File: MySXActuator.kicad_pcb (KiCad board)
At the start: 2 copper layers, 27.7 x 44 mm, 40 parts, among them J1 8P8C, Q1 2N7002, Q2 IRFR7546PbF, Q3 IRFR7546PbF, Q4 2N7002, Q5 BSS84A, U1 AP63205WU

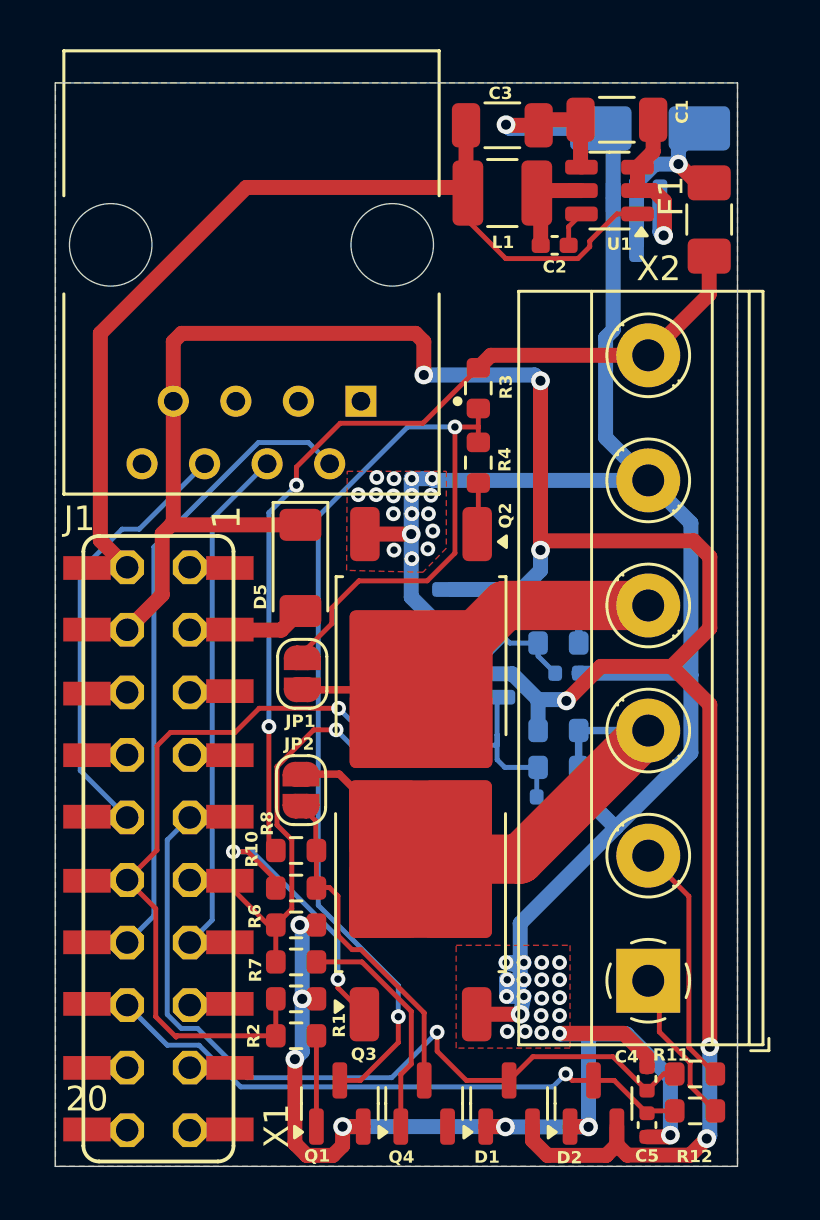
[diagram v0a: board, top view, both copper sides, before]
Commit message: add resistors to prevent led glowing when turned off
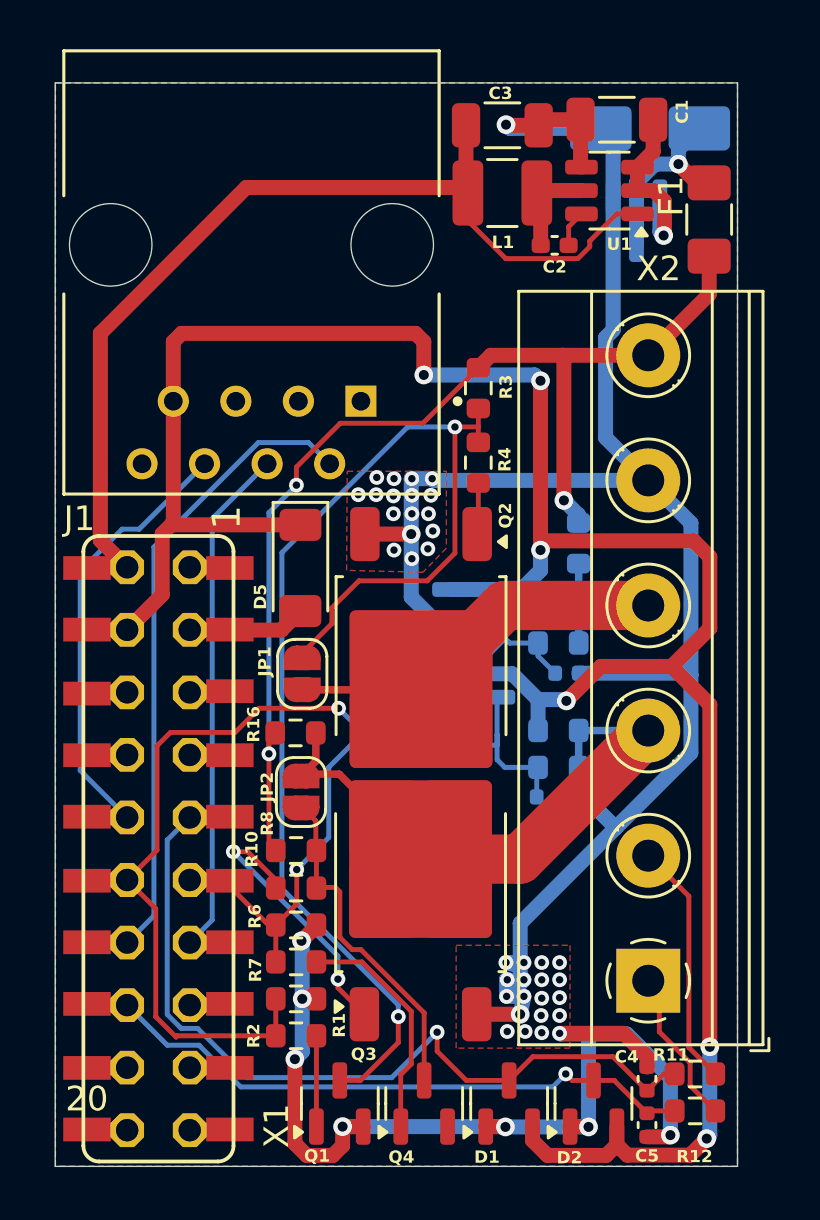
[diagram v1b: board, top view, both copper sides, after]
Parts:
- added R15: 22k, Resistor_SMD:R_0603_1608Metric, B.Cu at (156.6, 99.0)
- added R16: 22k, Resistor_SMD:R_0603_1608Metric, F.Cu at (145.1, 106.7)
- moved JP2 0.08 mm to (145.3, 109.0)
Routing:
- net VIN: track 37.5 -> 45.5 mm, vias 2 -> 3
- net D6_PWM: track 28.6 -> 26.4 mm
- net LED2: track 19.8 -> 21.8 mm
- net LED1: track 19.8 -> 21.5 mm
- net Net-(JP1-A): track 48.7 -> 49.9 mm
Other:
- board text added: "MySX Actuator v2.6"
- board text removed: "MySX Actuator v2.5"
